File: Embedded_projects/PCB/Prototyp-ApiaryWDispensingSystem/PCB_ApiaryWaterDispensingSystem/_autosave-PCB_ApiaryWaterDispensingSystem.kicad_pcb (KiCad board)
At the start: 2 copper layers, 217.3 x 127.3 mm, 255 parts, among them J1 Conn_02x01, J10 Conn_02x19_Odd_Even, J11 Conn_02x01, J12 Conn_02x01, J13 Conn_01x03, J14 Conn_01x02, J15 Conn_01x02, J16 Conn_02x01, J17 MSD-1-A, J18 Conn_01x02, J19 Conn_01x08, J2 Conn_01x04, J20 USB_B_Micro, J21 Conn_02x01, J3 Conn_02x01, J4 Conn_01x06, J5 Conn_01x03_Male, J6 Conn_02x01, J7 Conn_02x19_Odd_Even, J8 Conn_01x05_Male, J9 Conn_01x04_Male, Q1 Q_PMOS_GSD, Q2 Q_NPN_BEC, SW2 SW_Push, SW3 SW_Push, SW4 SW_Push, SW5 SW_Push, SW6 SW_Push, U1 STM32F411RETx, U10 LD3985M33R_SOT23, U11 STM32F103CBTx, U12 LD39050PU33, U2 24LC32, U3 DS3231M, U4 INA219AxD, U5 BME280, U6 INA219AxD, U7 drv8835, U8 LD1117S50TR_SOT223, U9 STS7PF30L, X1 Crystal, Y2 Crystal_GND23_Small, Y3 Crystal

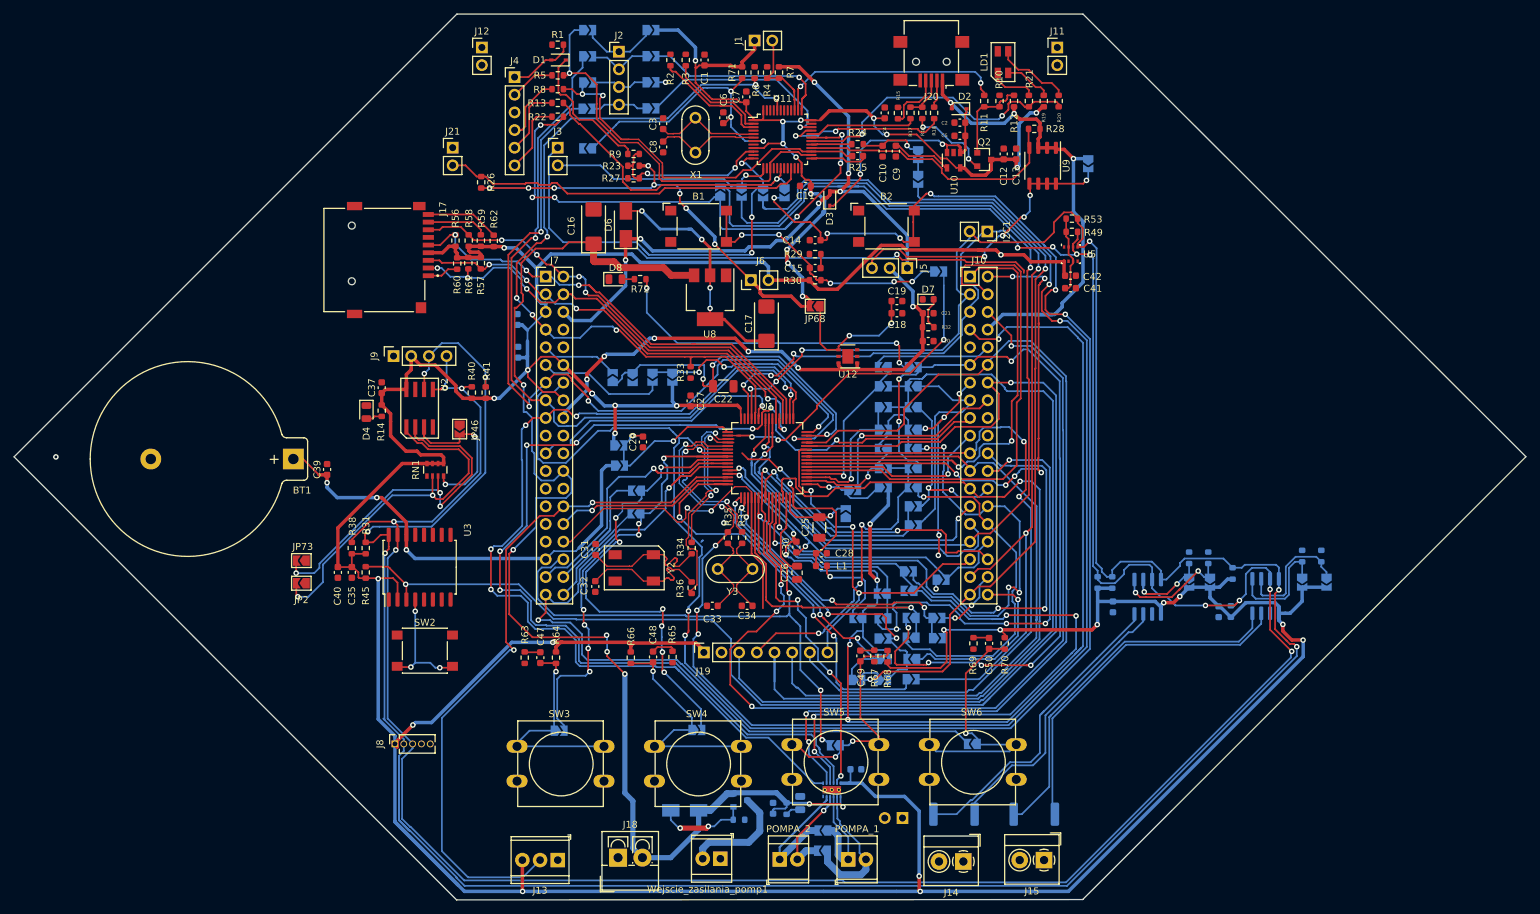
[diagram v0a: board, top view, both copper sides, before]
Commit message: update html in readme.RST and improved PCb #3
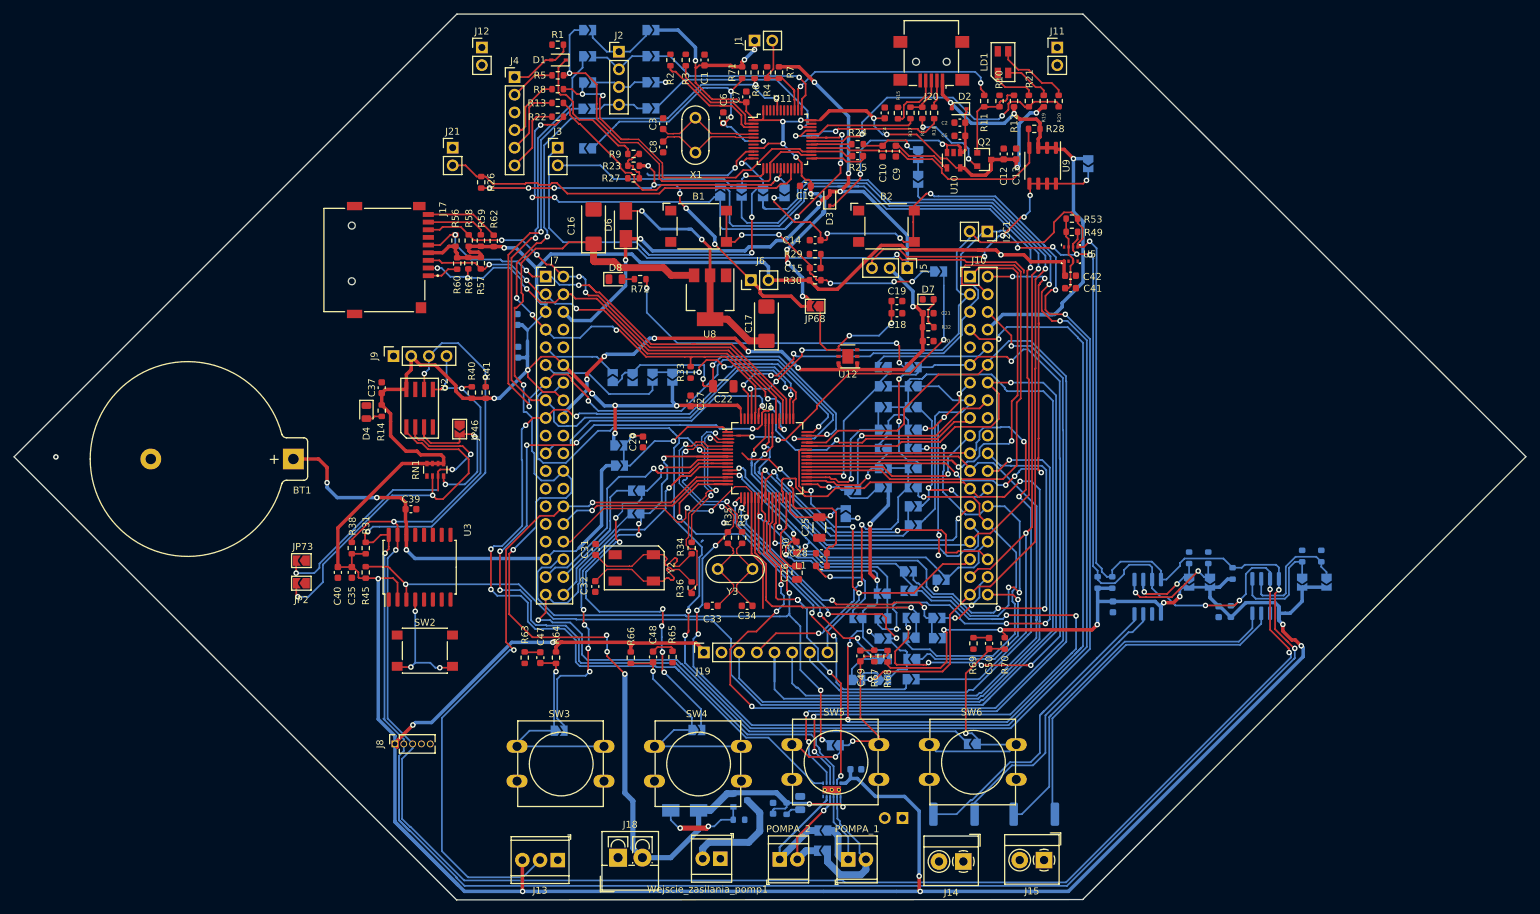
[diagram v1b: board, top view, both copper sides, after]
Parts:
- moved C39 13.3 mm to (100.5, 97.2), turned to 0 degrees
- turned C28 to 0 degrees
- turned L1 to 0 degrees
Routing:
- net Net-(JP73-Pad2): track 52.3 -> 46.3 mm
- net GND: track 3.64 -> 7.37 mm, vias 2 -> 4
- net BAT: track 65.7 -> 69.3 mm
- net AIN_1: track 24.7 -> 23.1 mm, vias 2 -> 1
- net Net-(JP57-Pad2): track 13.3 -> 14.3 mm
- net STM_JTCK: track 28.5 -> 27.6 mm
- net PB8: track 436.9 -> 436.1 mm
- net VDD: track 686.2 -> 685.5 mm
- net MODE: track 81.1 -> 81.3 mm, vias 4 -> 5
- net STM_RST: track 40.1 -> 40.0 mm, vias 3 -> 4
- net +3V3: vias 21 -> 23
- net Net-(C17-Pad1): vias 4 -> 2
